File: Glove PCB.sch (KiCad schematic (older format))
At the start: 26 parts, among them J1 USB_B_Micro, J2 Conn_01x06_Female, J3 Conn_01x04_Female, J5 Conn_01x06_Female, J7 Conn_02x07_Odd_Even, SW1 TS-1109S-B-B, U3 113990582

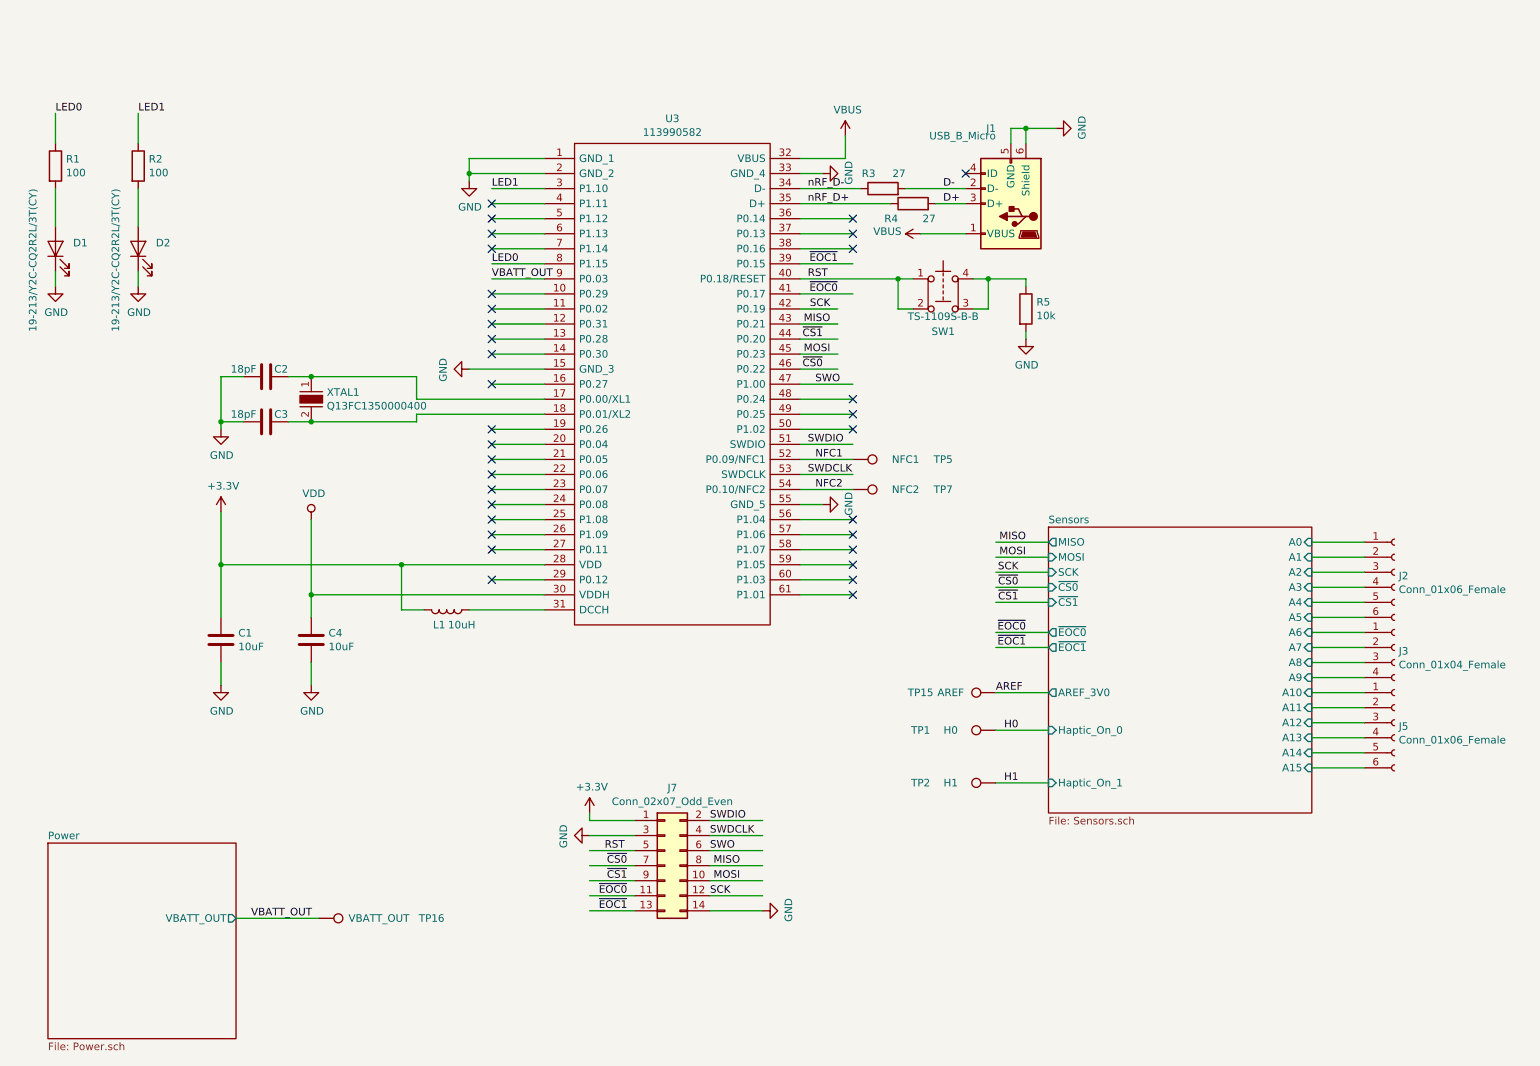
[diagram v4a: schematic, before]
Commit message: Added high side R for sensors and buck-boost. Replaced 3.0V VRef with LDO. BOM rev 1. Finished layout. TODO: Silkscreen.
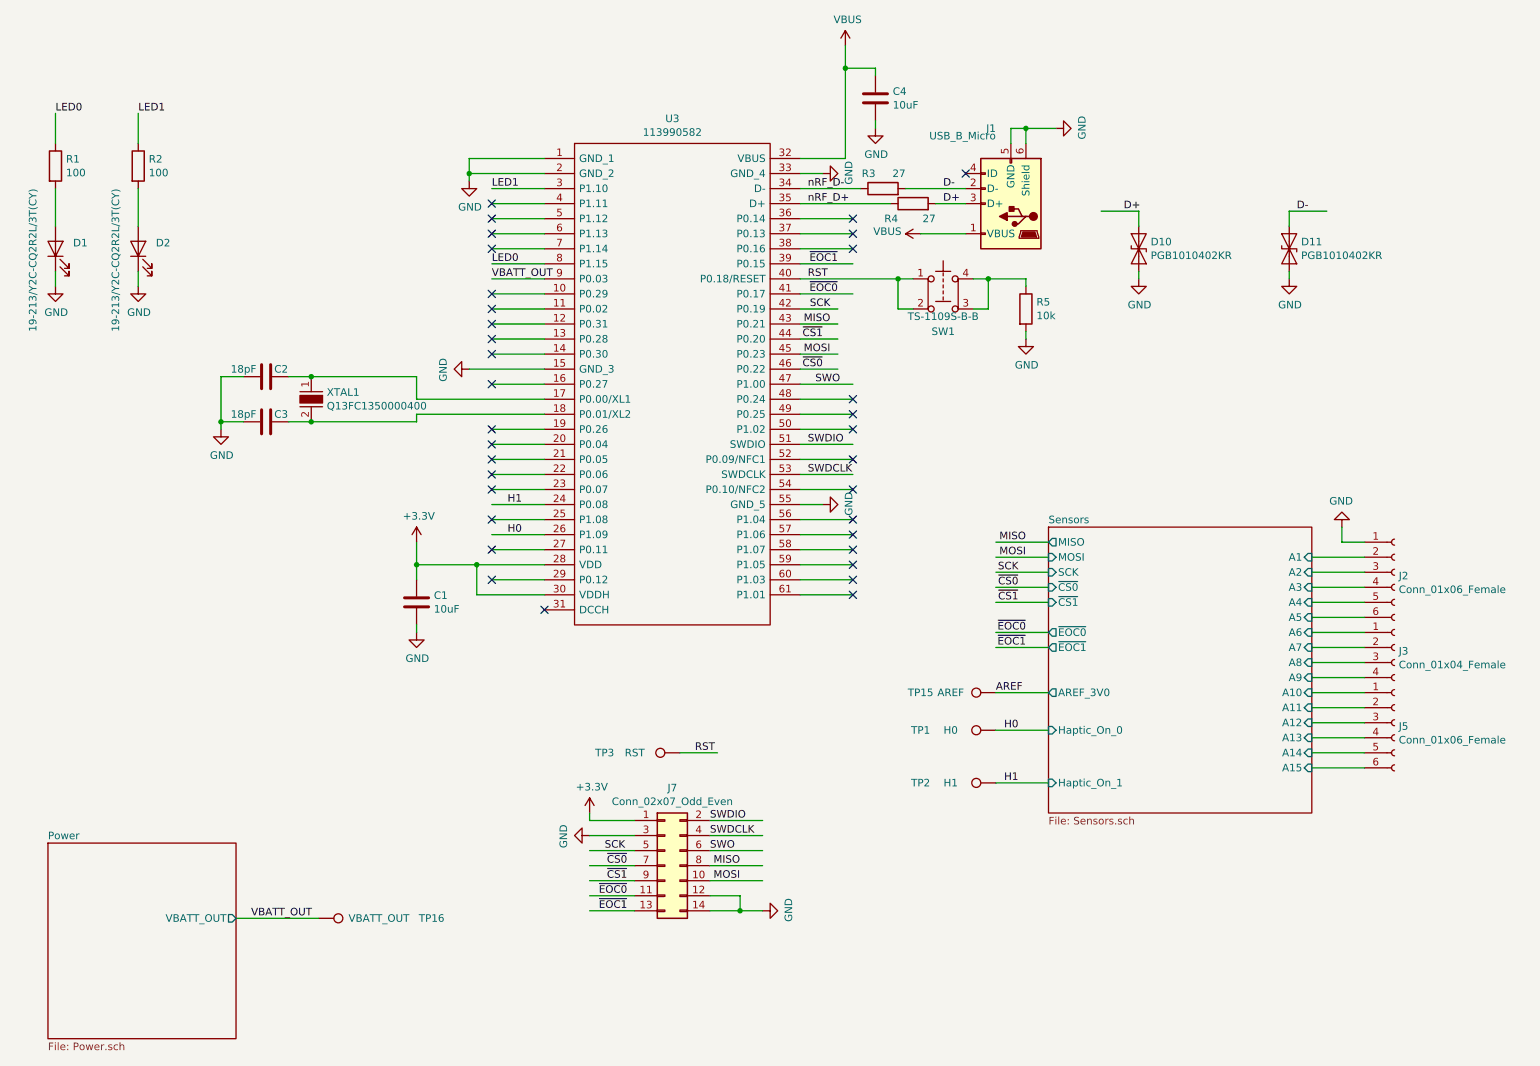
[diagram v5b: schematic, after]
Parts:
- removed L1: 10uH, Inductors_SMD:L_0805_HandSoldering, symbol Device:L
- removed TP5: NFC1, TestPoint:TestPoint_Pad_D1.5mm, symbol Connector:TestPoint
- removed TP7: NFC2, TestPoint:TestPoint_Pad_D1.5mm, symbol Connector:TestPoint
- added D10, D11: PGB1010402KR, Diode_SMD:D_0402_1005Metric, symbol Device:D_TVS
- added TP3: RST, TestPoint:TestPoint_Pad_D1.5mm, symbol Connector:TestPoint
- C1, C4: Description (none) -> MULTILAYER CERAMIC CAPACITORS MLCC - SMD/SMT 10UF 10V 0603 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; LCSC (none) -> C19702; MPN (none) -> CL10A106KP8NNNC; Manufacturer (none) -> Samsung Electro-Mechanics
- C2, C3: footprint Capacitor_SMD:C_0402_1005Metric -> Capacitors_SMD:C_0402; Description (none) -> MULTILAYER CERAMIC CAPACITORS MLCC - SMD/SMT 18PF 50V 0402 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; LCSC (none) -> C1549; MPN (none) -> 0402CG180J500NT; Manufacturer (none) -> Guangdong Fenghua Advanced Tech
- D1, D2: Description (none) -> LIGHT EMITTING DIODES (LED) YELLOW 585.5~591.5NM 90~180MCD@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; LCSC (none) -> C72038; MPN (none) -> 19-213/Y2C-CQ2R2L/3T(CY); Manufacturer (none) -> Everlight Elec
- J1, J2, J3, J5, J7, TP1, TP15, TP16, TP2: Description (none) -> -; LCSC (none) -> -; MPN (none) -> -; Manufacturer (none) -> -
- R1, R2: footprint Resistor_SMD:R_0603_1608Metric_Pad0.84x1.00mm_HandSolder -> Resistors_SMD:R_0603_HandSoldering; Description (none) -> CHIP RESISTOR - SURFACE MOUNT 100OHMS ±1% 1/10W 0603 ROHS; LCSC (none) -> C22775; MPN (none) -> 0603WAF1000T5E; Manufacturer (none) -> Uniroyal Elec
- R3, R4: Description (none) -> CHIP RESISTOR - SURFACE MOUNT 27OHMS ±1% 1/10W 0603 ROHS; LCSC (none) -> C25190; MPN (none) -> 0603WAF270JT5E; Manufacturer (none) -> Uniroyal Elec
- R5: footprint Resistor_SMD:R_0603_1608Metric_Pad0.84x1.00mm_HandSolder -> Resistor_SMD:R_0402_1005Metric; Description (none) -> CHIP RESISTOR - SURFACE MOUNT 10KOHMS ±1% 1/16W 0402 ROHS; LCSC (none) -> C25744; MPN (none) -> 0402WGF1002TCE; Manufacturer (none) -> Uniroyal Elec
- SW1: Description (none) -> SPST 50MA @ 12VDC VERTICAL ROUND BUTTON 160GF SMD TACTILE S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; LCSC (none) -> C480315; MPN (none) -> TS-1109S-B-B; Manufacturer (none) -> XKB Connectivity
- U3: LCSC (none) -> -; MPN (none) -> -; Manufacturer (none) -> -
- XTAL1: footprint SamacSys_Parts:ECX-31B -> Crystals:Crystal_SMD_G8-2pin_3.2x1.5mm; Description CRYSTAL 32.7680KHZ 12.5PF SMD -> SMD CRYSTAL RESONATORS 32.768KHZ ±20PPM SMD-3215_2P ROHS; LCSC (none) -> C32346; MPN ECS-.327-12.5-34B-TR -> Q13FC1350000400
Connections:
- net labels removed: NFC1, NFC2, VDD
- wire segments 147 -> 156
- no-connect marks 33 -> 34
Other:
- moved on the sheet: C1, C4
